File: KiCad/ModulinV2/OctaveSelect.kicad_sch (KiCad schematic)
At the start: 0 parts

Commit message: Modified Octave selector and started on waveform selection
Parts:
- added C29, C33, C35, C37, C39: 100n, symbol Device:C
- added C30, C34, C36, C38, C40: 1u, symbol Device:C
- added C31, C32: C, symbol Device:C
- added IC10, IC11, IC9: SN74LV10ADR, symbol SN74LV10ADR:SN74LV10ADRx3
- added IC12: SN74HC193DR, SOIC127P600X175-16N, symbol SN74HC193DR:SN74HC193DR
- added IC13: TMUX4051DYYRQ1, SOP50P326X110-16N, symbol TMUX4051DYYRQ1:TMUX4051DYYRQ1
- added R79, R80, R81, R84, R85, R86: 1k, symbol Device:R
- added R82, R83: R, symbol Device:R
- added SW4: ~, symbol RB14DE1100:RB14DE1100
- added U9: ~, symbol TL072HIDR:TL072HIDRx2
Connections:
- new net: R82.1, SW4.1
- new net: IC10.12, IC10.3
- new net: IC11.6, IC9.9
- new net: IC9.12, IC9.3
- new net: R81.1, R84.2
- new net: R83.1, SW4.3
- new net: IC9.5, IC9.8
- new net: IC10.9, IC11.8
- new net: IC10.5, IC10.8
- new net: IC11.12, IC9.11
- new net +12V: C39.2, C40.2, IC13.16 (VDD), U9.8 (V+)
- new net +1V: IC13.2 (S6), R85.1, R86.2
- new net +2V: IC13.4 (S7), R84.1, R85.2
- new net +3.3V: C29.2, C30.2, C33.2, C34.2, C35.2, C36.2, C37.2, C38.2, IC10.14 (VCC), IC11.14 (VCC), IC12.11 (~{LOAD}), IC12.16 (VCC), IC9.14 (VCC), SW4.2
- new net +3V: IC13.13 (S0), R80.1, R81.2
- new net +4V: IC13.14 (S1), R79.1, R80.2
- new net +5V: IC13.15 (S2), R79.2
- new net -12V: IC13.7 (VSS), U9.4 (V-)
- new net CLEAR: IC12.14 (CLR)
- new net DOWN: IC10.6, IC12.4 (DOWN)
- new net GND: C29.1, C30.1, C31.1, C32.1, C33.1, C34.1, C35.1, C36.1, C37.1, C38.1, C39.1, C40.1, IC10.7 (GND), IC11.7 (GND), IC12.1 (B), IC12.10 (C), IC12.15 (A), IC12.8 (GND), IC12.9 (D), IC13.6 (~{EN}), IC13.8 (GND), IC9.7 (GND), R86.1
- new net OCTAVE: IC13.3 (D), U9.3 (+), U9.5 (+)
- new net OCTAVE1: U9.1, U9.2 (-)
- new net OCTAVE2: U9.6 (-), U9.7
- new net QA: IC11.1, IC11.10, IC11.11, IC11.13, IC11.2, IC11.9, IC12.3 (QA), IC13.11 (A0)
- new net QB: IC10.10, IC12.2 (QB), IC13.10 (A1), IC9.10
- new net QC: IC10.11, IC11.3, IC11.4, IC11.5, IC12.6 (QC)
- new net QD: IC12.7 (QD), IC13.9 (A2)
- new net SW_DOWN: C32.2, IC10.4, IC9.1, IC9.13, IC9.2, R83.2
- new net SW_UP: C31.2, IC10.1, IC10.13, IC10.2, IC9.4, R82.2
- new net UP: IC12.5 (UP), IC9.6
- no-connect marks 0 -> 5
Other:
- note added: "Analog MUX"
- note added: "Binary counter"
- note added: "Output buffering"
- note added: "Power capacitors"
- note added: "Toggle switch"
- note added: "Up/down clock logic"
- note added: "V/Oct voltage divider"
- title: (none) -> Octave Selector

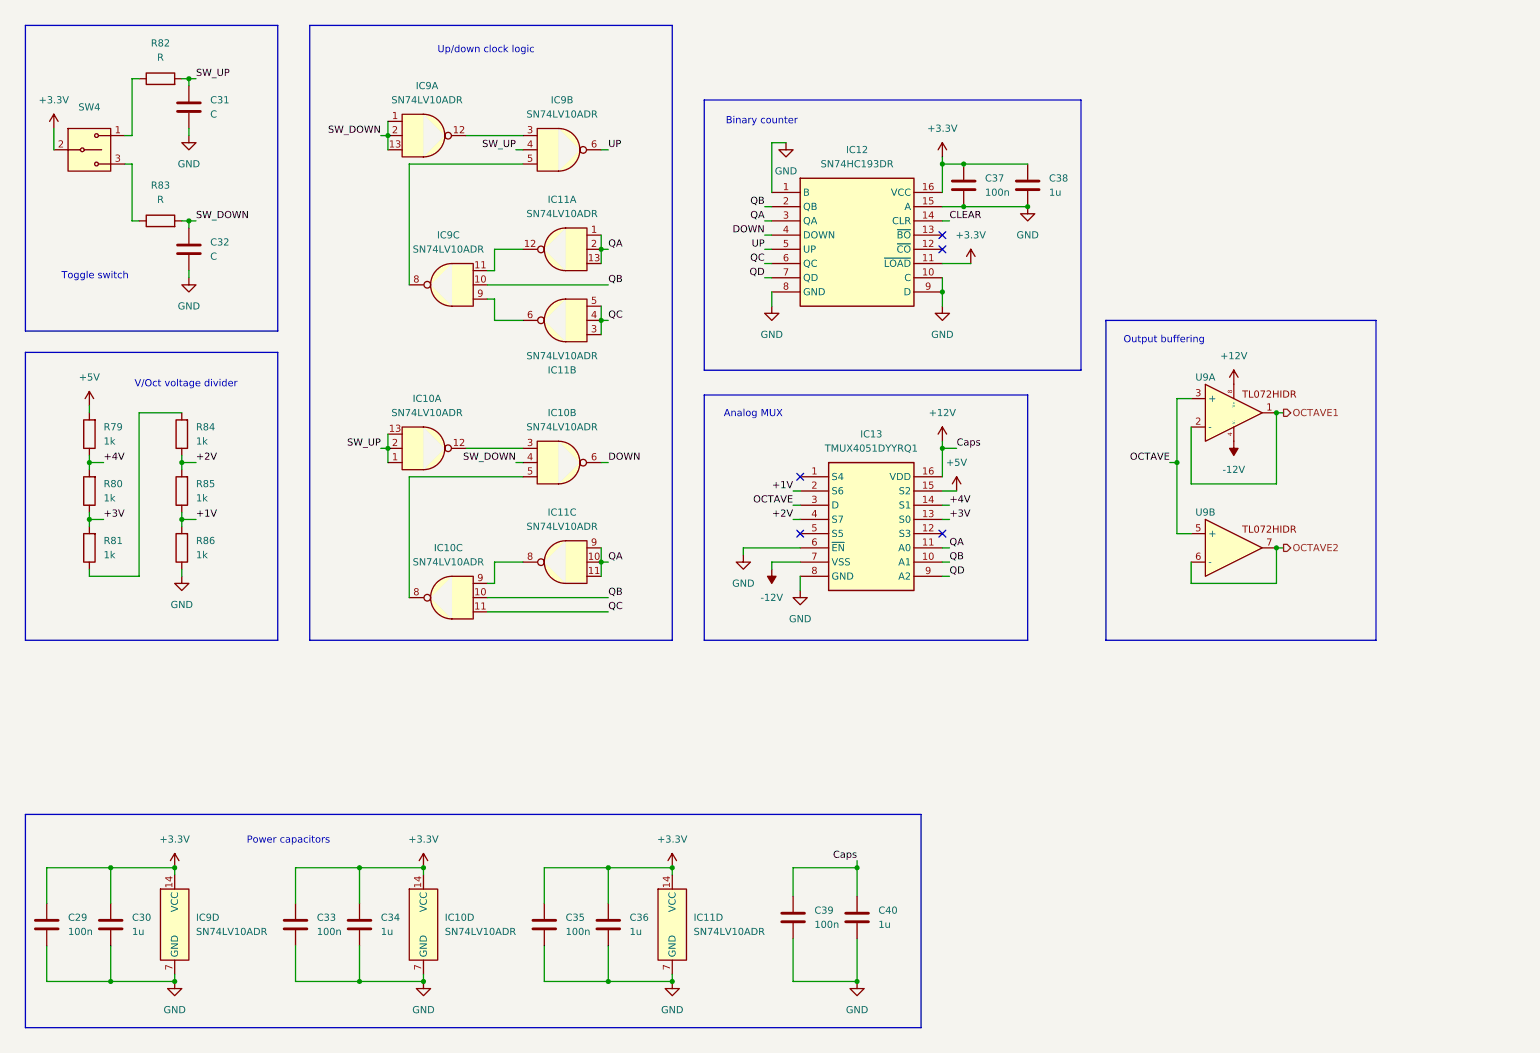
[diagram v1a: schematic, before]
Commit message: Modified USB connection and added LEDs
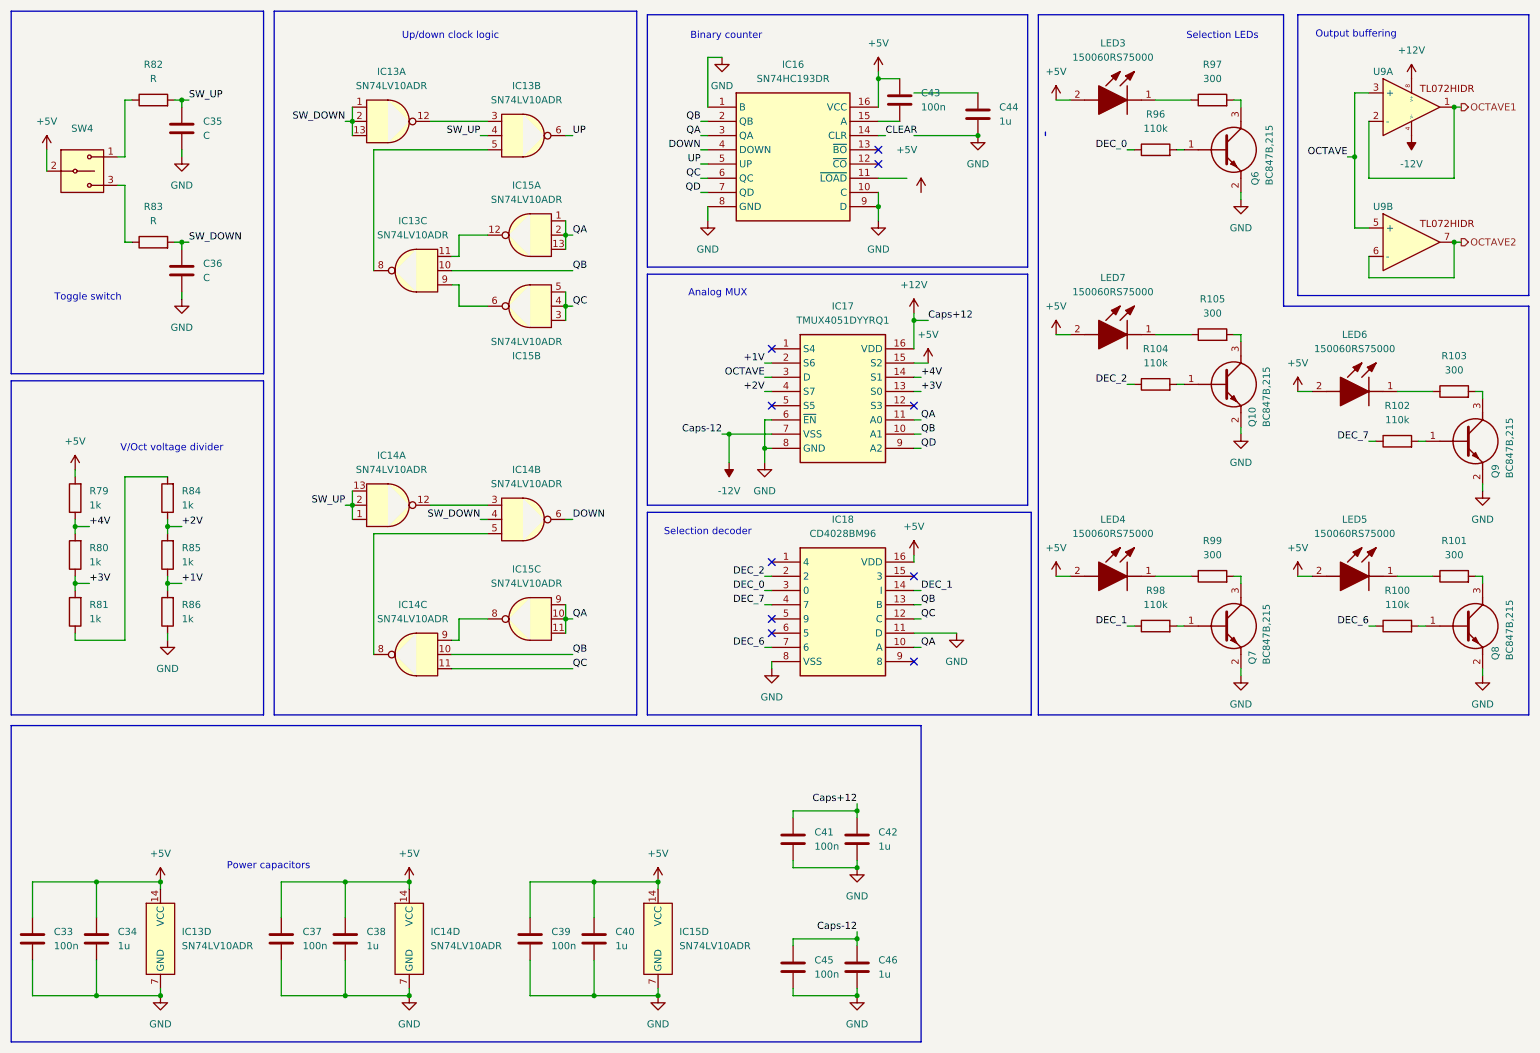
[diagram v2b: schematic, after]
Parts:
- added C45: 100n, symbol Device:C
- added C46: 1u, symbol Device:C
- added IC18: CD4028BM96, SOIC127P600X175-16N, symbol CD4028BM96:CD4028BM96
- added LED3, LED4, LED5, LED6, LED7: 150060RS75000, LEDC1608X80N, symbol 150060RS75000:150060RS75000
- added Q10, Q6, Q7, Q8, Q9: BC847B,215, BC847B215, symbol BC847B_215:BC847B,215
- added R100, R102, R104, R96, R98: 110k, symbol Device:R
- added R101, R103, R105, R97, R99: 300, symbol Device:R
- renumbered C29 to C33, C30 to C34, C31 to C35, C32 to C36, C33 to C37, C34 to C38, C35 to C39, C36 to C40, C39 to C41, C40 to C42, C37 to C43, C38 to C44, IC9 to IC13, IC10 to IC14, IC11 to IC15, IC12 to IC16, IC13 to IC17
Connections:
- net +5V: now also C33.2, C34.2, C37.2, C38.2, C39.2, C40.2, C43.2, IC13.14 (VCC), IC14.14 (VCC), IC15.14 (VCC), IC16.16 (VCC), SW4.2, IC18.16 (VDD), LED3.2 (A), LED4.2 (A), LED5.2 (A), LED6.2 (A), LED7.2 (A)
- net -12V: now also C45.2, C46.2
- net GND: now also C45.1, C46.1, IC18.11 (D), IC18.8 (VSS), Q10.2 (E), Q6.2 (E), Q7.2 (E), Q8.2 (E), Q9.2 (E); no longer C43.1, IC16.15 (A)
- net QA: now also IC18.10 (A)
- net QB: now also IC18.13 (B)
- net QC: now also IC18.12 (C)
- removed net +3.3V: C33.2, C34.2, C37.2, C38.2, C39.2, C40.2, C43.2, C44.2, IC13.14 (VCC), IC14.14 (VCC), IC15.14 (VCC), IC16.11 (~{LOAD}), IC16.16 (VCC), SW4.2
- new net: LED6.1 (K), R103.1
- new net: LED3.1 (K), R97.1
- new net: Q6.3 (C), R97.2
- new net: Q8.1 (B), R100.2
- new net: Q7.1 (B), R98.2
- new net: Q7.3 (C), R99.2
- new net: LED4.1 (K), R99.1
- new net: C43.1, IC16.15 (A)
- new net: Q10.1 (B), R104.2
- new net: Q10.3 (C), R105.2
- new net: LED5.1 (K), R101.1
- new net: Q8.3 (C), R101.2
- new net: LED7.1 (K), R105.1
- new net: Q9.1 (B), R102.2
- new net: Q9.3 (C), R103.2
- new net: Q6.1 (B), R96.2
- new net DEC_0: IC18.3 (0), R96.1
- new net DEC_1: IC18.14 (I), R98.1
- new net DEC_2: IC18.2, R104.1
- new net DEC_6: IC18.7 (6), R100.1
- new net DEC_7: IC18.4 (7), R102.1
- no-connect marks 5 -> 10
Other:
- note added: "Selection LEDs"
- note added: "Selection decoder"
- moved on the sheet: C33, C34, C35, C36, C37, C38, C39, C40, C41, C42, C43, C44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

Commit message: Fleshed out the waveform select schematic a bit + general cleanup
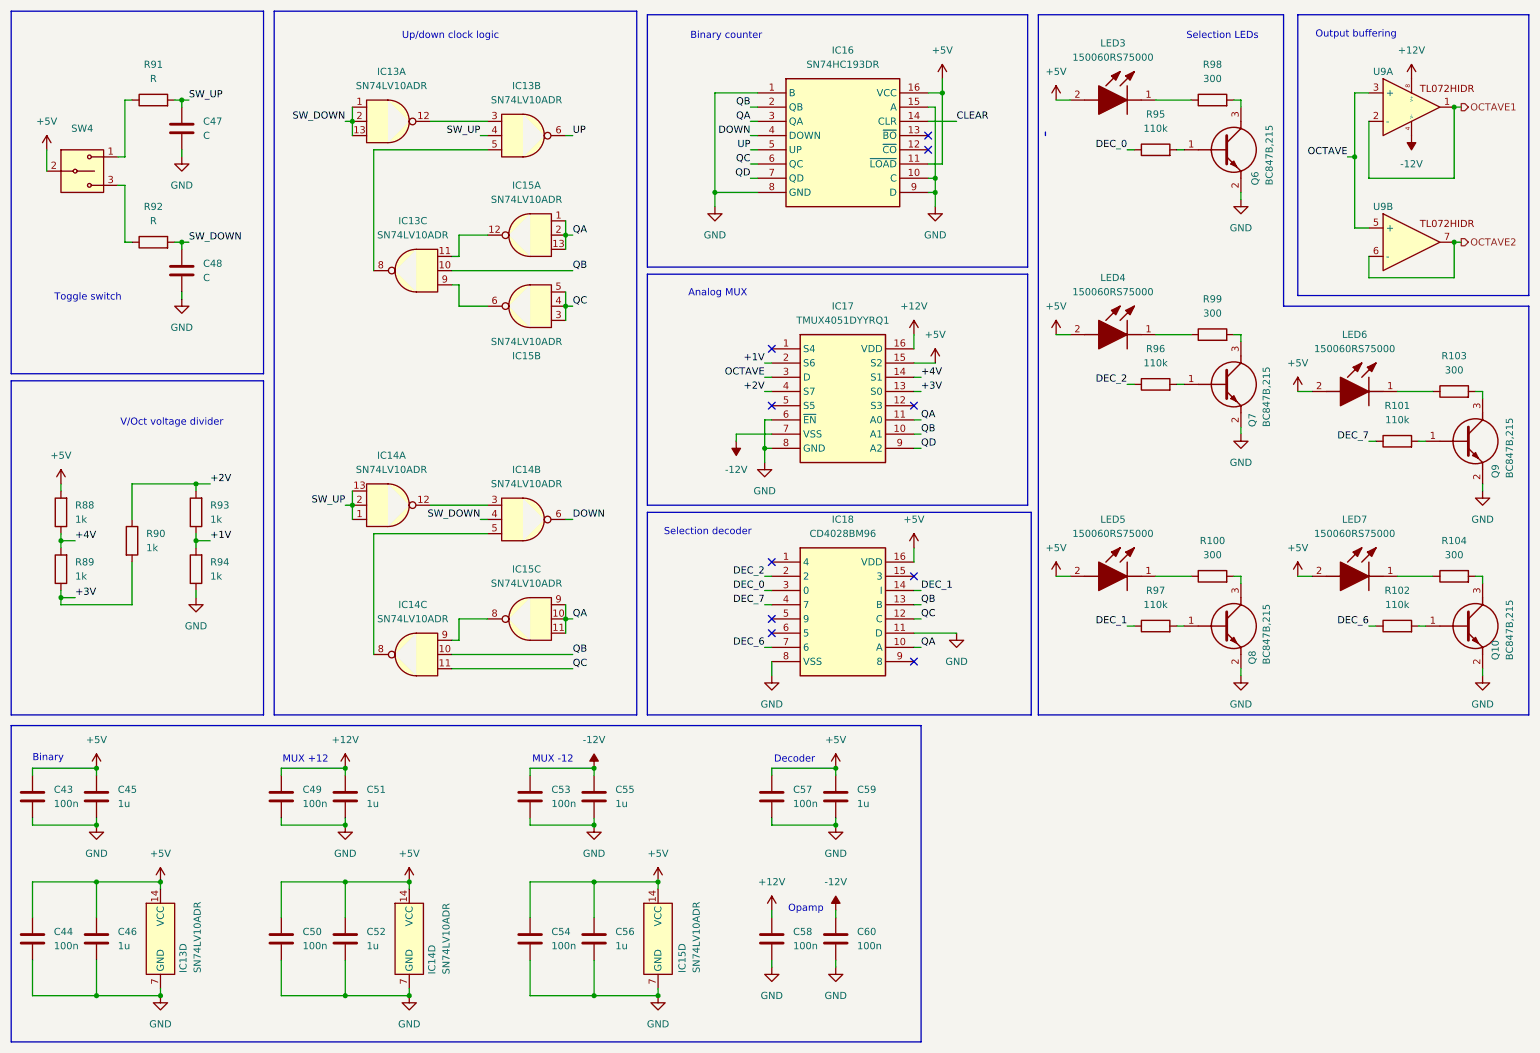
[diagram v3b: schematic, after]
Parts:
- removed R81: 1k, symbol Device:R
- added C57, C58, C60: 100n, symbol Device:C
- added C59: 1u, symbol Device:C
- renumbered C33 to C44, C44 to C45, C34 to C46, C35 to C47, C36 to C48, C41 to C49, C37 to C50, C42 to C51, C38 to C52, C45 to C53, C39 to C54, C46 to C55, C40 to C56, LED7 to LED4, LED4 to LED5, LED5 to LED7, Q8 to Q10, Q10 to Q7, Q7 to Q8, R99 to R100, R102 to R101, R100 to R102, R101 to R104, R79 to R88, R80 to R89, R84 to R90, R82 to R91, R83 to R92, R85 to R93, R86 to R94, R96 to R95, R104 to R96, R98 to R97, R97 to R98, R105 to R99
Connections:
- net +12V: now also C58.2
- net +3V: now also R90.2
- net +5V: now also C45.2, IC16.11 (~{LOAD}), C57.2, C59.2
- net -12V: now also C60.2
- net GND: now also C43.1, IC16.15 (A), C57.1, C58.1, C59.1, C60.1
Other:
- note added: "Binary"
- note added: "Decoder"
- note added: "MUX +12"
- note added: "MUX -12"
- note added: "Opamp"
- note removed: "Power capacitors"
- moved on the sheet: C43, C45, C49, C51, C53, C55, IC16, R88, R89, R90, R93, R94

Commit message: Added initial power supply schematic and modified MCU components
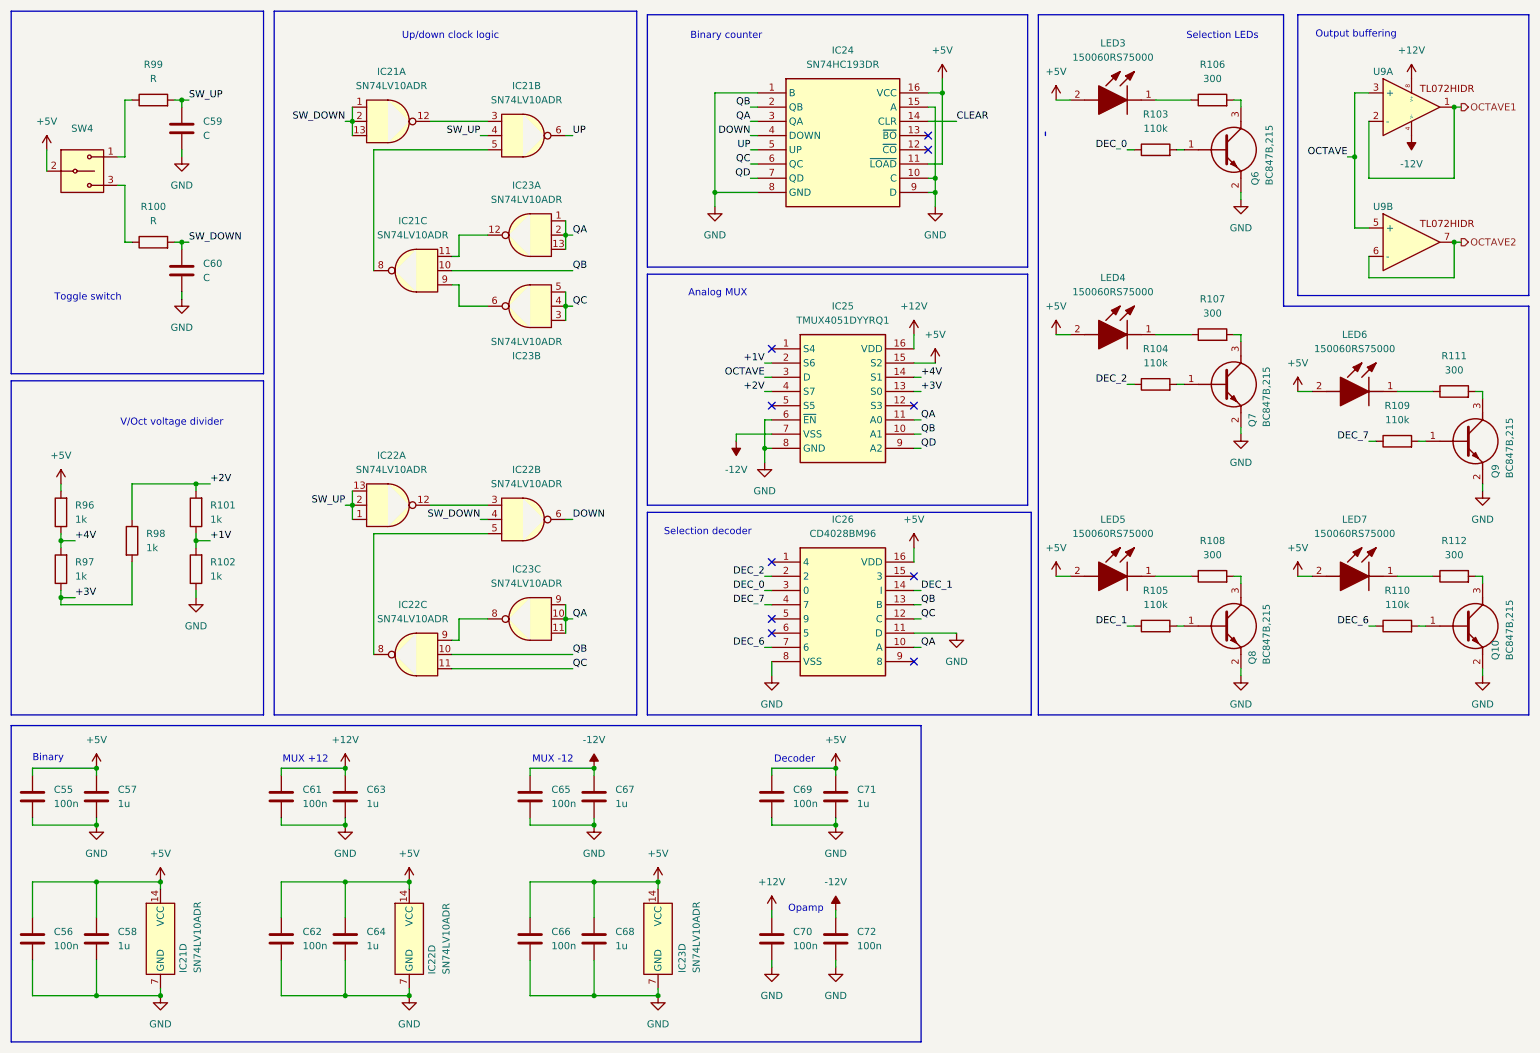
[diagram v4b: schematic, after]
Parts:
- renumbered C43 to C55, C44 to C56, C45 to C57, C46 to C58, C47 to C59, C48 to C60, C49 to C61, C50 to C62, C51 to C63, C52 to C64, C53 to C65, C54 to C66, C55 to C67, C56 to C68, C57 to C69, C58 to C70, C59 to C71, C60 to C72, IC13 to IC21, IC14 to IC22, IC15 to IC23, IC16 to IC24, IC17 to IC25, IC18 to IC26, R92 to R100, R93 to R101, R94 to R102, R95 to R103, R96 to R104, R97 to R105, R98 to R106, R99 to R107, R100 to R108, R101 to R109, R102 to R110, R103 to R111, R104 to R112, R88 to R96, R89 to R97, R90 to R98, R91 to R99

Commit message: Designed ADSR and better tuning schematics with digital/manual capability
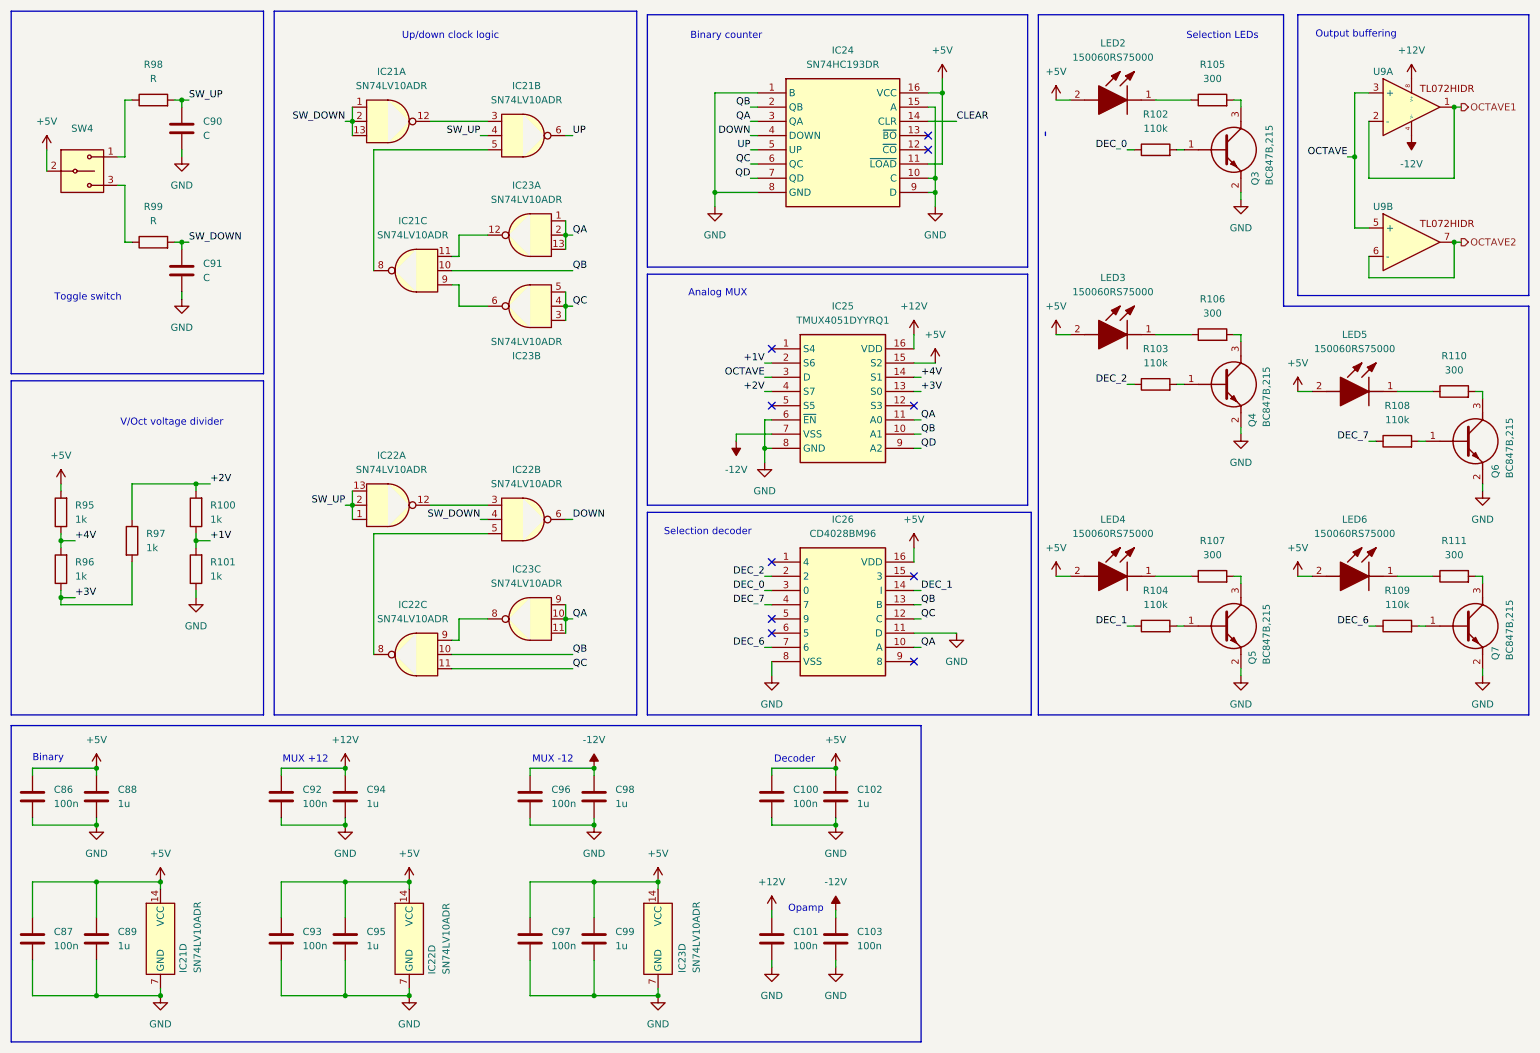
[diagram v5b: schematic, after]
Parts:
- renumbered C69 to C100, C70 to C101, C71 to C102, C72 to C103, C55 to C86, C56 to C87, C57 to C88, C58 to C89, C59 to C90, C60 to C91, C61 to C92, C62 to C93, C63 to C94, C64 to C95, C65 to C96, C66 to C97, C67 to C98, C68 to C99, LED3 to LED2, LED4 to LED3, LED5 to LED4, LED6 to LED5, LED7 to LED6, Q6 to Q3, Q7 to Q4, Q8 to Q5, Q9 to Q6, Q10 to Q7, R101 to R100, R102 to R101, R103 to R102, R104 to R103, R105 to R104, R106 to R105, R107 to R106, R108 to R107, R109 to R108, R110 to R109, R111 to R110, R112 to R111, R96 to R95, R97 to R96, R98 to R97, R99 to R98, R100 to R99
